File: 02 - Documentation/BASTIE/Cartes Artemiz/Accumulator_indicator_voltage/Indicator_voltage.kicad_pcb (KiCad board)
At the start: 2 copper layers, 82.4 x 42.6 mm, 22 parts, among them J7 2P Droit 2-11-2022, Q1 NMOS SQ2348ES-T1_GE3

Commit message: Revert "Delete kicad_prl"
This reverts commit 9fe5be2906406c3c64afc6048a7ffd3d023d0e3c.
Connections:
- PS1 pad 4: 0 -> unconnected-(PS1-TRIM-Pad4)
- PS1 pad 6: 0 -> unconnected-(PS1-REMOTE_ON/OFF-Pad6)
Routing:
- net 0: track 109.1 -> 103.9 mm
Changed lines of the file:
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@@
 	(net 13 "Net-(R13-Pad2)")
 	(net 14 "Net-(R14-Pad1)")
+	(net 15 "unconnected-(PS1-TRIM-Pad4)")
+	(net 16 "unconnected-(PS1-REMOTE_ON{slash}OFF-Pad6)")
 	(footprint "EPSA_lib:RESC3216X70N"
 		(layer "F.Cu")
@@
 			)
 		)
+		(sheetname "Racine")
+		(sheetfile "Indicator_voltage.kicad_sch")
 		(attr smd)
 		(fp_line
@@
 			)
 		)
+		(sheetname "Racine")
+		(sheetfile "Indicator_voltage.kicad_sch")
 		(attr smd)
 		(fp_line
@@
 			)
 		)
+		(sheetname "Racine")
+		(sheetfile "Indicator_voltage.kicad_sch")
 		(attr smd)
 		(fp_line
@@
 			)
 		)
+		(sheetname "Racine")
+		(sheetfile "Indicator_voltage.kicad_sch")
 		(attr through_hole)
 		(fp_line
@@
 			)
 		)
+		(sheetname "Racine")
+		(sheetfile "Indicator_voltage.kicad_sch")
 		(attr smd)
 		(fp_line
@@
 			)
 		)
+		(sheetname "Racine")
+		(sheetfile "Indicator_voltage.kicad_sch")
 		(attr smd)
 		(fp_line
@@
 			)
 		)
+		(sheetname "Racine")
+		(sheetfile "Indicator_voltage.kicad_sch")
 		(attr through_hole)
 		(fp_line
@@
 			(layers "*.Cu" "*.Mask")
 			(remove_unused_layers no)
-			(net 2 "0")
+			(net 15 "unconnected-(PS1-TRIM-Pad4)")
 			(pinfunction "TRIM")
 			(pintype "passive")
@@
 			(layers "*.Cu" "*.Mask")
 			(remove_unused_layers no)
-			(net 2 "0")
+			(net 16 "unconnected-(PS1-REMOTE_ON{slash}OFF-Pad6)")
 			(pinfunction "REMOTE_ON/OFF")
 			(pintype "passive")
@@
 			)
 		)
+		(sheetname "Racine")
+		(sheetfile "Indicator_voltage.kicad_sch")
 		(attr smd)
 		(fp_line
@@
 			)
 		)
+		(sheetname "Racine")
+		(sheetfile "Indicator_voltage.kicad_sch")
 		(attr smd)
 		(fp_line
@@
 			)
 		)
+		(sheetname "Racine")
+		(sheetfile "Indicator_voltage.kicad_sch")
 		(attr smd)
 		(fp_line
@@
 			)
 		)
+		(sheetname "Racine")
+		(sheetfile "Indicator_voltage.kicad_sch")
 		(attr smd)
 		(fp_line
@@
 			)
 		)
+		(property ki_fp_filters "Pin* Test*")
+		(sheetname "Racine")
+		(sheetfile "Indicator_voltage.kicad_sch")
 		(attr exclude_from_pos_files)
 		(fp_line
@@
 			)
 		)
+		(sheetname "Racine")
+		(sheetfile "Indicator_voltage.kicad_sch")
 		(attr smd)
 		(fp_line
@@
 			)
 		)
+		(sheetname "Racine")
+		(sheetfile "Indicator_voltage.kicad_sch")
 		(attr smd)
 		(fp_line
@@
 			)
 		)
+		(sheetname "Racine")
+		(sheetfile "Indicator_voltage.kicad_sch")
 		(attr smd)
 		(fp_line
@@
 			)
 		)
+		(property ki_fp_filters "Pin* Test*")
+		(sheetname "Racine")
+		(sheetfile "Indicator_voltage.kicad_sch")
 		(attr exclude_from_pos_files)
 		(fp_line
@@
 			)
 		)
+		(sheetname "Racine")
+		(sheetfile "Indicator_voltage.kicad_sch")
 		(attr smd)
 		(fp_line
@@
 			)
 		)
+		(sheetname "Racine")
+		(sheetfile "Indicator_voltage.kicad_sch")
 		(attr smd)
 		(fp_line
@@
 			)
 		)
+		(sheetname "Racine")
+		(sheetfile "Indicator_voltage.kicad_sch")
 		(attr smd)
 		(fp_line
@@
 	)
 	(segment
-		(start 106.85 113.71)
-		(end 110.6 117.46)
-		(width 0.6)
-		(layer "F.Cu")
-		(net 2)
-	)
-	(segment
 		(start 94.05 124.55)
 		(end 94 124.5)
@@
 	)
 	(segment
-		(start 137.53 114.92)
-		(end 128 124.45)
+		(start 104.95 112.05)
+		(end 105.85 112.05)
 		(width 0.6)
 		(layer "F.Cu")
@@
 	)
 	(segment
-		(start 98.5 124.55)
-		(end 94.05 124.55)
+		(start 105.85 118.225)
+		(end 110.6 122.975)
 		(width 0.6)
 		(layer "F.Cu")
@@
 	)
 	(segment
-		(start 156.32 114.92)
-		(end 137.53 114.92)
+		(start 98.5 124.55)
+		(end 94.05 124.55)
 		(width 0.6)
 		(layer "F.Cu")
@@
 	)
 	(segment
-		(start 104.95 112.05)
-		(end 105.85 112.05)
-		(width 0.6)
-		(layer "F.Cu")
-		(net 2)
-	)
-	(segment
-		(start 110.6 117.46)
-		(end 110.6 122.975)
+		(start 105.85 112.05)
+		(end 110.6 107.3)
 		(width 0.6)
 		(layer "F.Cu")
@@
 	)
 	(segment
-		(start 162.5 108.74)
-		(end 156.32 114.92)
-		(width 0.6)
-		(layer "F.Cu")
-		(net 2)
-	)
-	(segment
-		(start 106.85 111.05)
-		(end 110.6 107.3)
+		(start 147.69 104.76)
+		(end 128 124.45)
 		(width 0.6)
 		(layer "F.Cu")
@@
 	)
 	(segment
-		(start 105.85 112.05)
-		(end 106.85 111.05)
+		(start 156.32 104.76)
+		(end 147.69 104.76)
 		(width 0.6)
 		(layer "F.Cu")
@@
 	)
 	(segment
-		(start 106.85 111.05)
-		(end 106.85 113.71)
+		(start 112.2 124)
+		(end 127.55 124)
 		(width 0.6)
 		(layer "F.Cu")
@@
 	)
 	(segment
-		(start 112.2 124)
-		(end 127.55 124)
+		(start 127.55 124)
+		(end 128 124.45)
 		(width 0.6)
 		(layer "F.Cu")
@@
 	)
 	(segment
-		(start 127.55 124)
-		(end 128 124.45)
+		(start 105.85 112.05)
+		(end 105.85 118.225)
 		(width 0.6)
 		(layer "F.Cu")

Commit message: Routage Voltage Indicator
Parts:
- removed the ? at (93.0, 107.0)
- removed the ? at (165.5, 97.0)
- removed the ? at (165.0, 125.5)
- removed PS1: Alim HP EC7BW18-72S12, EPSA_lib:EC7BW1872S12
- removed R11, R13: 390k, EPSA_lib:RESC3216X70N
- added ?: , , F.Cu at (38.8, 101.6)
- added ?: , , F.Cu at (116.6, 45.6)
- added ?: , , F.Cu at (38.8, 45.6)
- added ?: , , F.Cu at (116.6, 101.8)
- added C1: 0.1u 630V, EPSA_lib:CAPC4532X200N, F.Cu at (82.6, 54.4)
- added C10: 10u, EPSA_lib:CAPC2012X130N, F.Cu at (64.6, 99.6)
- added C2: 10p 630V, EPSA_lib:CAPC3216X100N, F.Cu at (63.0, 76.4)
- added C3: 0.1u, EPSA_lib:CAPC2012X130N, F.Cu at (83.0, 72.2)
- added C4: 0.1u, EPSA_lib:CAPC2012X130N, F.Cu at (78.4, 69.0)
- added C5: 10u, EPSA_lib:CAPC2012X130N, F.Cu at (71.0, 76.8)
- added C6: 10u, EPSA_lib:GRM31x, F.Cu at (69.0, 82.0)
- added C7: 47u, EPSA_lib:CAPC3225X270N, F.Cu at (91.2, 56.4)
- added C8: 47u, EPSA_lib:CAPC3225X270N, F.Cu at (95.4, 56.4)
- added C9: 47u, EPSA_lib:CAPC3225X270N, F.Cu at (99.4, 56.4)
- added D1: Diode CMDSH2-3_TR_PBFREE, EPSA_lib:SOD2512X110N, F.Cu at (80.7, 84.8)
- added D2: Diode US1KFA, EPSA_lib:SODFL3618X143N, F.Cu at (86.4, 82.0)
- added D3: Diode US1KFA, EPSA_lib:SODFL3618X143N, F.Cu at (84.8, 60.6)
- added F1: 200mA, EPSA_lib:0ADAP0200RE, F.Cu at (107.3, 46.2)
- added IC1: Contrôleur LT8316EFE#PBF, EPSA_lib:LT8315EFEPBF, F.Cu at (70.2, 70.0)
- added L1: 1m, EPSA_lib:WE-PD_1260_1245_1280_121054, F.Cu at (97.8, 72.7)
- added Q2: NMOS TK3P80E_RQ, EPSA_lib:TK3P80ERQ, F.Cu at (73.6, 61.4)
- added R10: 2.4k, EPSA_lib:RESC3216X70N, F.Cu at (75.8, 80.2)
- added U1: Alim LP TSR_0.5-2450, EPSA_lib:TSR-0.5-2433, F.Cu at (105.7, 87.0)
- added Z1: Diode Zener CMHZ4107_TR_PBFREE, EPSA_lib:SOD3816X135N, F.Cu at (104.2, 56.8)
- R2: value 390k -> 10k
- R3: value 390k -> 0.22; footprint EPSA_lib:RESC3216X70N -> EPSA_lib:RESC1608X55N
- R8: value 5k6 -> 22k
- R9: value 3k9 -> 22k
- moved R2 118.4 mm to (54.6, 75.7), turned to 0 degrees
- moved R14 104.5 mm to (53.2, 87.8), turned to 90 degrees
- moved R6 94.2 mm to (54.8, 94.2), turned to 180 degrees
- moved R3 94.0 mm to (80.8, 59.6), turned to 0 degrees
- moved R12 81.6 mm to (61.4, 94.2), turned to 180 degrees
- moved TP1 79.5 mm to (116.2, 56.8)
- moved R4 69.6 mm to (68.8, 89.4), turned to 180 degrees
- moved CP1 53.3 mm to (68.6, 95.2), turned to 180 degrees
- moved R1 47.0 mm to (82.6, 92.6)
- moved R9 46.2 mm to (81.2, 80.2), turned to 0 degrees
- moved R5 44.2 mm to (74.6, 91.0), turned to 90 degrees
- moved TP3 42.9 mm to (116.2, 87.8)
- moved R8 37.6 mm to (78.4, 72.2), turned to 0 degrees
- moved R7 27.7 mm to (82.6, 97.2), turned to 0 degrees
- moved Q1 18.0 mm to (91.4, 98.2), turned to 0 degrees
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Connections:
- CP1 pad 5: 5V -> +5V
- J7 pad 1: 12V -> +12V
- R1 pad 1: 5V -> +5V
- R2 pad 1: Net-(R13-Pad2) -> HV+
- R3 pad 1: 0 -> Net-(IC1-SENSE)
- R3 pad 2: /150V -> Net-(D3-K)
- R8 pad 1: 12V -> Net-(IC1-VC)
- R8 pad 2: 5V -> Net-(C3-Pad1)
- R9 pad 1: 5V -> Net-(IC1-FB)
- R9 pad 2: 0 -> Net-(D1-A)
- TP1 pad 1: HV+ -> HV in
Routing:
- net +12V: track 0.00 -> 85.2 mm
- net HV+: track 17.9 -> 83.1 mm
- net Net-(D3-K): track 0.00 -> 64.1 mm
- net +5V: track 0.00 -> 44.1 mm, vias 0 -> 2
- net 5V: track 44.1 -> 0.00 mm, vias 3 -> 0
- net 0: track 103.9 -> 133.8 mm, vias 0 -> 4
- net Net-(IC1-EN/UVLO): track 0.00 -> 25.4 mm, vias 0 -> 2
- net Net-(D1-K): track 0.00 -> 24.2 mm
- net 12V: track 23.8 -> 0.00 mm
- net HV in: track 0.00 -> 15.1 mm
- net /150V: track 13.8 -> 0.00 mm
- net Net-(IC1-SENSE): track 0.00 -> 13.1 mm
- net Net-(CP1-IN+): track 21.9 -> 9.24 mm
- net Net-(IC1-FB): track 0.00 -> 12.2 mm
- net Net-(IC1-GATE): track 0.00 -> 8.20 mm
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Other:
- board size 82.4 x 42.6 mm -> 91.8 x 70.2 mm

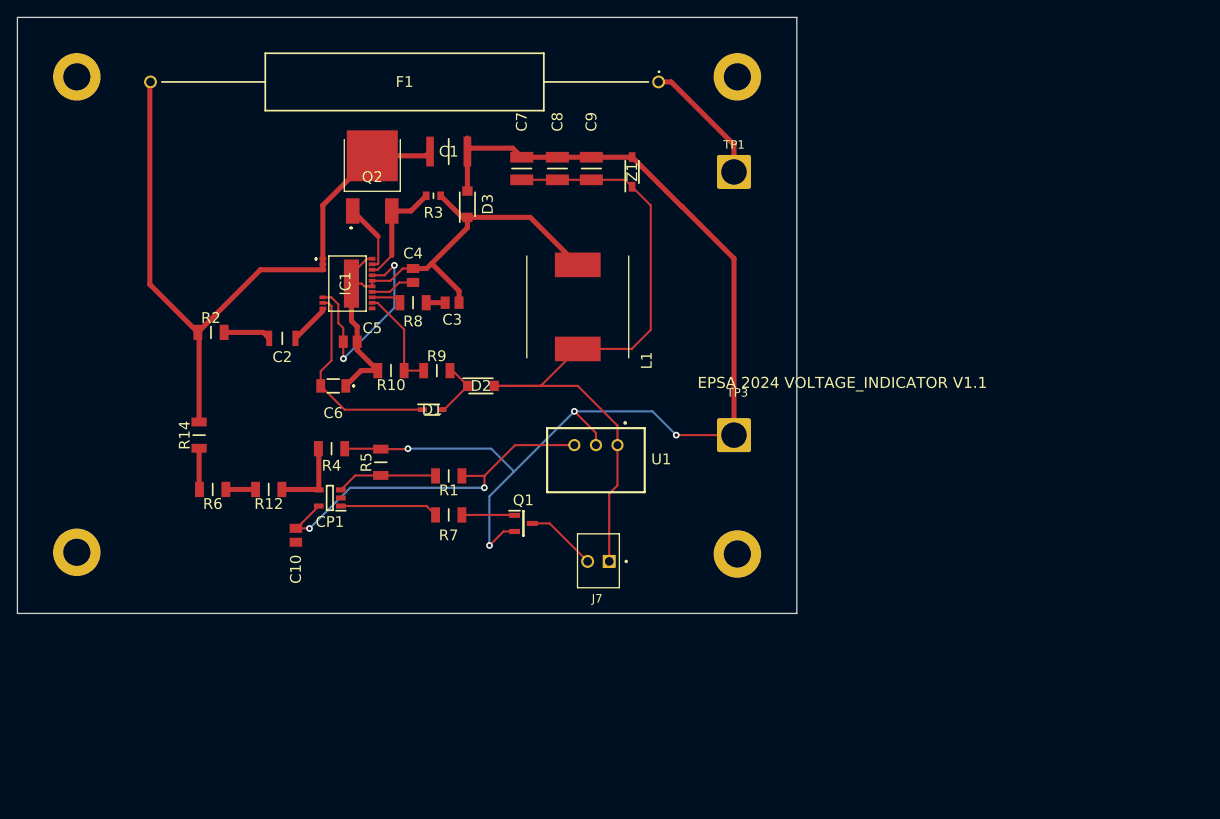
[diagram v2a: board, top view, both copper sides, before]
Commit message: Ajout compo convertisseur 600V + IMD SCS + BOM AIR
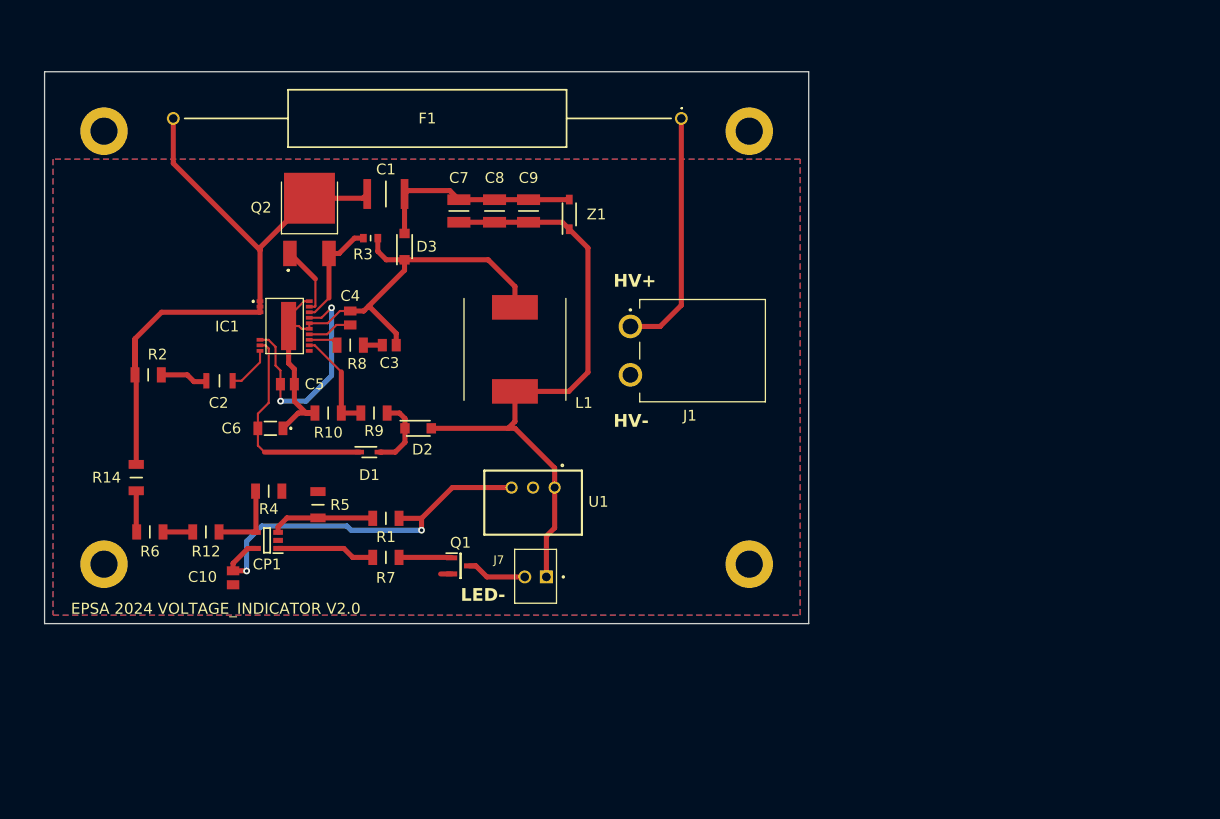
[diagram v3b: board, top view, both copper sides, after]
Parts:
- removed the ? at (38.8, 101.6)
- removed the ? at (116.6, 45.6)
- removed the ? at (38.8, 45.6)
- removed the ? at (116.6, 101.8)
- removed TP1, TP3: type="R" model="TestPoint" lib="", Connector_Wire:SolderWire-2.5sqmm_1x01_D2.4mm_OD3.6mm
- added ?: , , F.Cu at (118.0, 103.0)
- added ?: , , F.Cu at (42.0, 52.0)
- added ?: , , F.Cu at (42.0, 103.0)
- added ?: , , F.Cu at (118.0, 52.0)
- added J1: 2P Angle HV 200241-1212, EPSA_lib:2002411212, F.Cu at (104.0, 75.0)
- moved C3 8.93 mm to (75.6, 77.2)
- moved C4 8.93 mm to (71.0, 74.0)
- moved C7 8.93 mm to (83.8, 61.4)
- moved C8 8.93 mm to (88.0, 61.4)
- moved C9 8.93 mm to (92.0, 61.4)
- moved D1 8.93 mm to (73.2, 89.8)
- moved D2 8.93 mm to (79.0, 87.0)
- moved Q1 8.93 mm to (84.0, 103.2)
- moved R14 8.93 mm to (45.8, 92.8)
- moved R8 8.93 mm to (71.0, 77.2)
- moved R9 8.93 mm to (73.8, 85.2)
- moved U1 8.93 mm to (98.3, 92.0)
- moved Z1 8.93 mm to (96.8, 61.8)
- moved C2 8.93 mm to (55.6, 81.4)
- moved C5 8.93 mm to (63.6, 81.8)
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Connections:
- F1 pad 1: HV in -> Net-(F1-Pad1)
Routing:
- net 0: track 133.8 -> 26.1 mm, vias 4 -> 0
- net Net-(F1-Pad1): track 0.00 -> 29.0 mm
- net HV in: track 15.1 -> 0.00 mm
- net +12V: track 85.2 -> 75.0 mm
- net HV+: track 83.1 -> 77.6 mm
- net +5V: track 44.1 -> 47.1 mm
- net Net-(D3-K): track 64.1 -> 67.0 mm
- net Net-(IC1-EN/UVLO): track 25.4 -> 27.2 mm
- net Net-(D1-A): track 7.06 -> 8.70 mm
- net LED-: track 8.37 -> 7.05 mm
- net Net-(D1-K): track 24.2 -> 25.4 mm
- net Net-(IC1-DCM): track 4.86 -> 5.48 mm
- added copper zone on B.Cu, net 0
- added copper zone on F.Cu, net 0
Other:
- board size 91.8 x 70.2 mm -> 90 x 65 mm
- board text added: "EPSA 2024 VOLTAGE_INDICATOR V2.0"
- board text added: "HV+"
- board text added: "HV-"
- board text added: "LED+"
- board text added: "LED-"
- board text removed: "EPSA 2024 VOLTAGE_INDICATOR V1.1"
